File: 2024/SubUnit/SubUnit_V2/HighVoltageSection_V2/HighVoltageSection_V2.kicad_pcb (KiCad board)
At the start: 2 copper layers, 62.2 x 24.4 mm, 17 parts, among them J1 Conn_01x02_Socket, J10 Conn_01x02_Socket, J2 Conn_01x02_Socket, J3 Conn_01x02_Socket, J4 Conn_01x02_Socket, J6 Conn_01x02_Socket, J7 Conn_01x02_Socket, Q2 NMOS, Q3 NMOS

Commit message: あとシルクとDRC通すだけ
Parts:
- removed the G*** at (7.62, -4.83)
- added G***: LOGO, rione_ssl:sslcircuitQR15, B.Cu at (7.49, -4.70)
- moved C8 12.4 mm to (-6.86, -2.01), turned to 90 degrees
- moved J10 6.68 mm to (-15.0, -6.60), turned to -90 degrees
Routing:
- net VOUT: track 0.00 -> 19.9 mm, vias 0 -> 50
- net CHIP: track 36.7 -> 40.9 mm
- net STRAIGHT: track 6.82 -> 9.93 mm
- net source1: vias 0 -> 99

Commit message: 完成
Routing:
- net VOUT: vias 50 -> 49
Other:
- board text added: "CAPACITOR"
- board text added: "GND"
- board text added: "SOLENOID"
- board text added: "VOUT"
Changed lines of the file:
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@@
         (effects (font (size 1 1) (thickness 0.15)))
     )
-    (fp_text user "${REFERENCE}" (at 0 1.27) (layer "F.Fab")
-        (effects (font (size 1 1) (thickness 0.15)))
-    )
     (fp_line (start -1.33 -1.33) (end 0 -1.33)
       (stroke (width 0.12) (type solid)) (layer "F.SilkS"))
@@
     (property "ki_keywords" "R res resistor")
     (attr smd)
-    (fp_text reference "R9" (at 3 0 90) (layer "B.SilkS")
+    (fp_text reference "R9" (at 0.016 1.474 90) (layer "B.SilkS")
         (effects (font (size 1 1) (thickness 0.15)) (justify mirror))
     )
@@
         (effects (font (size 1 1) (thickness 0.1)) (justify mirror))
     )
-    (fp_text value "NMOS" (at 0 -1 90 unlocked) (layer "B.Fab")
+    (fp_text value "NMOS" (at 0 -1 90 unlocked) (layer "B.Fab") hide
         (effects (font (size 1 1) (thickness 0.15)) (justify mirror))
     )
@@
         (effects (font (size 1 1) (thickness 0.1)) (justify left bottom mirror))
     )
-    (fp_text user "${REFERENCE}" (at 0 -2.5 90 unlocked) (layer "B.Fab")
-        (effects (font (size 1 1) (thickness 0.15)) (justify mirror))
-    )
     (fp_text user "drain" (at -2 -5 90 unlocked) (layer "B.Fab")
         (effects (font (size 1 1) (thickness 0.1)) (justify left bottom mirror))
@@
         (effects (font (size 1 1) (thickness 0.15)) (justify mirror))
     )
-    (fp_text user "${REFERENCE}" (at 1.25 2.4 90) (layer "B.Fab")
-        (effects (font (size 1 1) (thickness 0.15)) (justify mirror))
-    )
     (fp_line (start -2.86 -2.21) (end -0.45 -2.21)
       (stroke (width 0.12) (type solid)) (layer "B.SilkS"))
@@
     (property "ki_keywords" "R res resistor")
     (attr smd)
-    (fp_text reference "R8" (at 0 1.5 90) (layer "B.SilkS")
+    (fp_text reference "R8" (at 0 -1.474 90) (layer "B.SilkS")
         (effects (font (size 1 1) (thickness 0.15)) (justify mirror))
     )
@@
     (property "ki_keywords" "diode TVS voltage suppressor")
     (attr smd)
-    (fp_text reference "D2" (at 0.038184 -2.119906 135) (layer "B.SilkS")
+    (fp_text reference "D2" (at -1.093187 2.046367 135) (layer "B.SilkS") hide
         (effects (font (size 1 1) (thickness 0.15)) (justify mirror))
     )
@@
     (property "ki_keywords" "R res resistor")
     (attr smd)
-    (fp_text reference "R10" (at 0 -1.25 -270) (layer "B.SilkS")
+    (fp_text reference "R10" (at 0.032 1.474 -270) (layer "B.SilkS")
         (effects (font (size 1 1) (thickness 0.15)) (justify mirror))
     )
@@
     (property "ki_keywords" "R res resistor")
     (attr smd)
-    (fp_text reference "R11" (at 3.25 0 -270) (layer "B.SilkS")
+    (fp_text reference "R11" (at 0.016 -1.474 -270) (layer "B.SilkS")
         (effects (font (size 1 1) (thickness 0.15)) (justify mirror))
     )
@@
   (gr_line locked (start -13.019294 2.790812) (end -0.000004 2.790812)
     (stroke (width 0.2) (type solid)) (layer "Edge.Cuts"))
+  (gr_text "SOLENOID" (at 17.399 6.35 -45) (layer "B.SilkS")
+    (effects (font (size 0.7 0.7) (thickness 0.14) bold italic) (justify left bottom mirror))
+  )
+  (gr_text "GND" (at 23.876 -7.62) (layer "B.SilkS")
+    (effects (font (size 0.7 0.7) (thickness 0.14) bold italic) (justify left bottom mirror))
+  )
+  (gr_text "CAPACITOR" (at -20.066 -5.588) (layer "B.SilkS")
+    (effects (font (size 0.7 0.7) (thickness 0.14) bold italic) (justify left bottom mirror))
+  )
+  (gr_text "CAPACITOR" (at 25.908 -5.588) (layer "B.SilkS")
+    (effects (font (size 0.7 0.7) (thickness 0.14) bold italic) (justify left bottom mirror))
+  )
+  (gr_text "VOUT" (at -21.336 -7.62) (layer "B.SilkS")
+    (effects (font (size 0.7 0.7) (thickness 0.14) bold italic) (justify left bottom mirror))
+  )
+  (gr_text "SOLENOID" (at -13.589 2.54 45) (layer "B.SilkS")
+    (effects (font (size 0.7 0.7) (thickness 0.14) bold italic) (justify left bottom mirror))
+  )
   (gr_text "BoostCircuitHighVoltageSection3.0\n20240505\nKotaroOCHIISHI" (at 0.254 -1.397) (layer "B.SilkS")
     (effects (font (size 0.7 0.7) (thickness 0.1) italic) (justify left bottom mirror))
@@
   (via (at -5.842 0.508) (size 0.8) (drill 0.4) (layers "F.Cu" "B.Cu") (net 2))
   (via (at -24.892 10.16) (size 0.8) (drill 0.4) (layers "F.Cu" "B.Cu") (free) (net 2))
-  (via (at -17.526 -10.922) (size 2) (drill 1.5) (layers "F.Cu" "B.Cu") (free) (net 2))
   (via (at 25.4 9.906) (size 0.8) (drill 0.4) (layers "F.Cu" "B.Cu") (free) (net 2))
   (via (at 23.368 11.684) (size 0.8) (drill 0.4) (layers "F.Cu" "B.Cu") (free) (net 2))

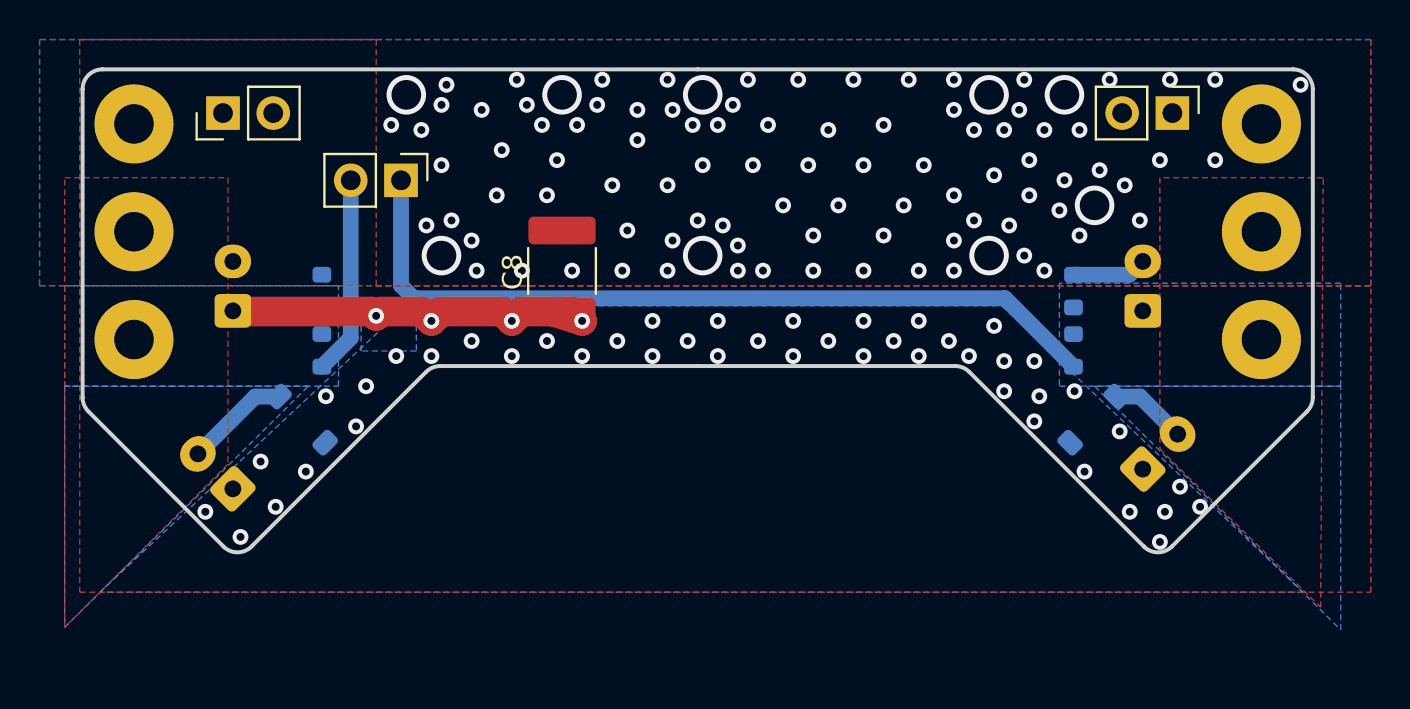
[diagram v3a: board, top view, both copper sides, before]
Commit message: hvsの干渉を直した
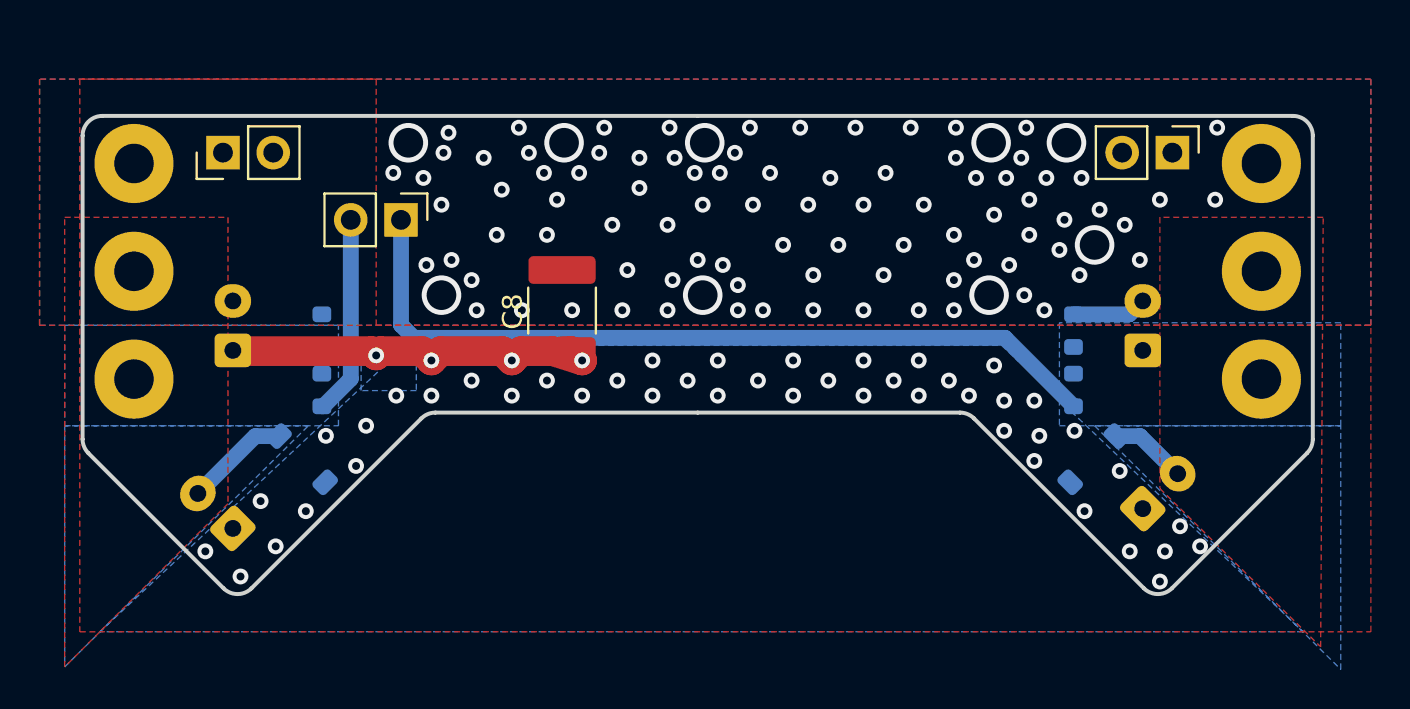
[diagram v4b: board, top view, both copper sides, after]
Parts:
- moved D2 2.00 mm to (-20.0, 7.50)
- moved D3 2.00 mm to (20.0, 7.50)
- moved G*** 2.00 mm to (7.49, -2.70)
- moved J1 2.00 mm to (-24.0, -8.00)
- moved J10 2.00 mm to (-15.0, -4.60)
- moved J2 2.00 mm to (24.0, -8.00)
- moved J3 2.00 mm to (-23.5, 2.00)
- moved J4 2.00 mm to (22.5, 2.00)
- moved J6 2.00 mm to (-23.5, 11.0)
- moved J7 2.00 mm to (22.5, 10.0)
- moved Q2 2.00 mm to (-28.5, -2.00)
- moved Q3 2.00 mm to (28.5, -2.00)
- moved R10 2.00 mm to (19.0, 4.00)
- moved R11 2.00 mm to (19.0, 1.00)
- moved R8 2.00 mm to (-19.0, 4.00)
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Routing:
- net source1: vias 99 -> 96
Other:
- board size 62.2 x 24.4 mm -> 62.2 x 24.2 mm
